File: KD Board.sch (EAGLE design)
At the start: 10 parts, among them IC1 LM555D

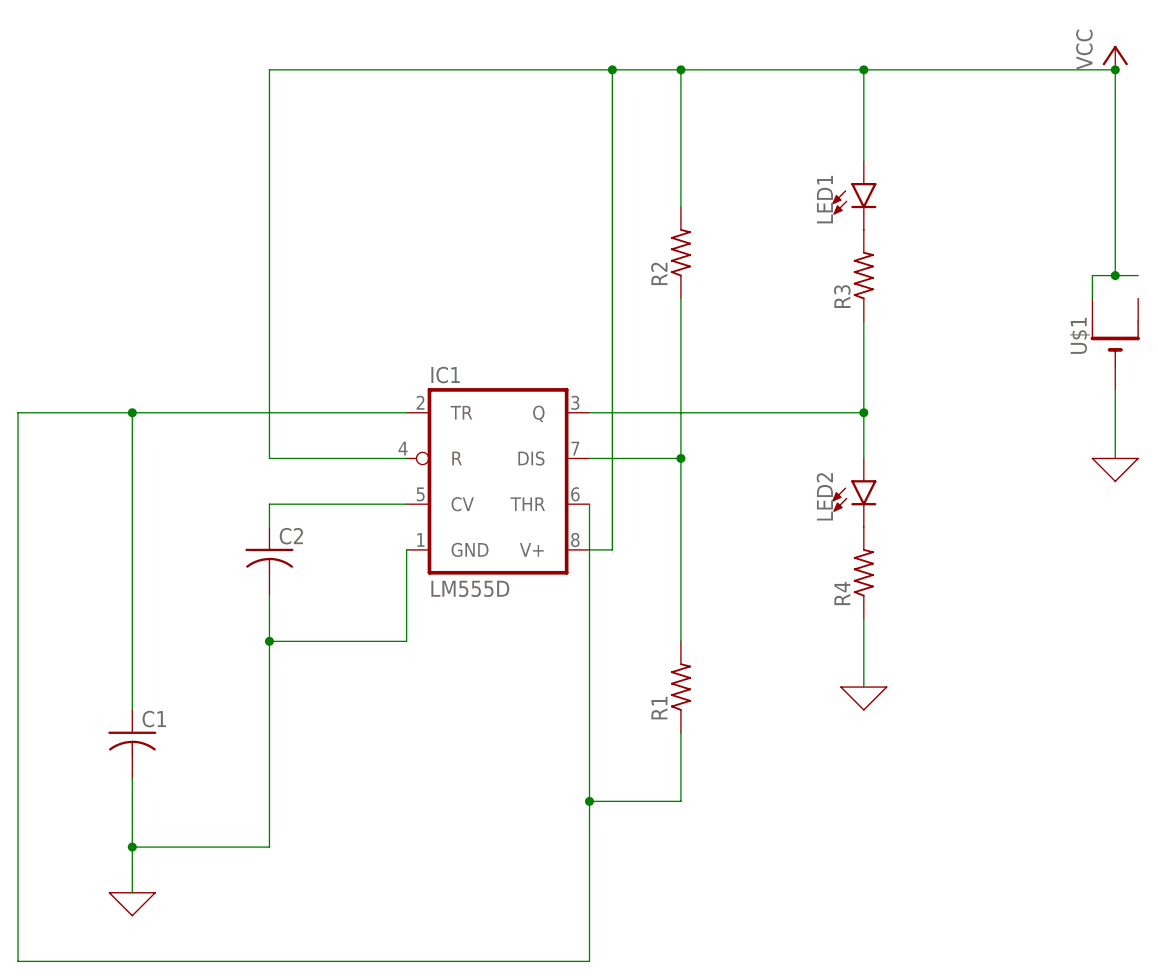
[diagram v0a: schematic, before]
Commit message: Moved name to silk layer. Board not square. Minor fixes.
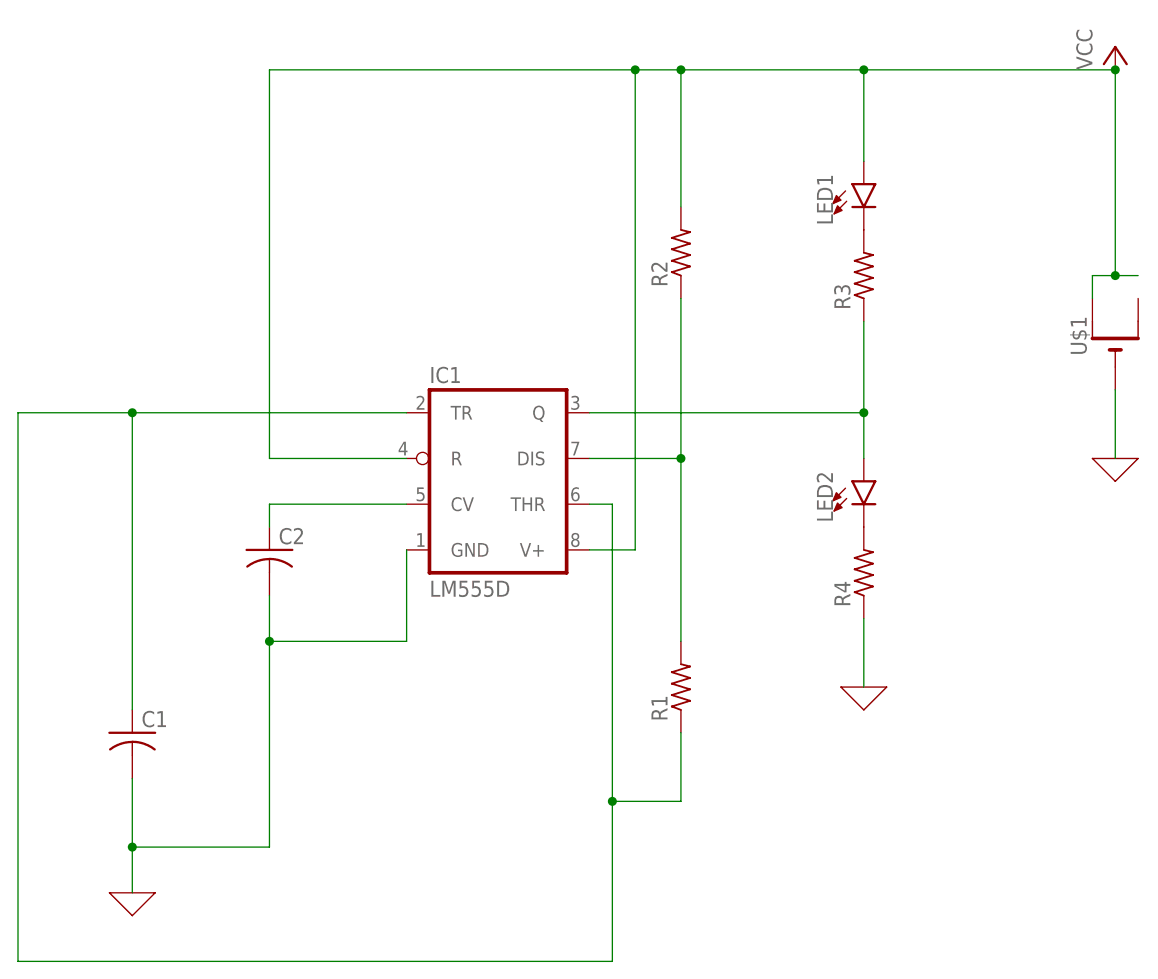
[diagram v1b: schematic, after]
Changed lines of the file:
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@@
 <wire x1="-10.16" y1="58.42" x2="-22.86" y2="58.42" width="0.1524" layer="91"/>
 <wire x1="-22.86" y1="58.42" x2="-22.86" y2="-2.54" width="0.1524" layer="91"/>
-<wire x1="-22.86" y1="-2.54" x2="40.64" y2="-2.54" width="0.1524" layer="91"/>
+<wire x1="-22.86" y1="-2.54" x2="43.18" y2="-2.54" width="0.1524" layer="91"/>
 <pinref part="IC1" gate="A" pin="THR"/>
-<wire x1="40.64" y1="48.26" x2="40.64" y2="15.24" width="0.1524" layer="91"/>
+<wire x1="40.64" y1="48.26" x2="43.18" y2="48.26" width="0.1524" layer="91"/>
+<wire x1="43.18" y1="48.26" x2="43.18" y2="15.24" width="0.1524" layer="91"/>
 <pinref part="R1" gate="G$1" pin="1"/>
-<wire x1="40.64" y1="15.24" x2="50.8" y2="15.24" width="0.1524" layer="91"/>
+<wire x1="43.18" y1="15.24" x2="50.8" y2="15.24" width="0.1524" layer="91"/>
 <wire x1="50.8" y1="15.24" x2="50.8" y2="22.86" width="0.1524" layer="91"/>
-<junction x="40.64" y="15.24"/>
-<wire x1="40.64" y1="-2.54" x2="40.64" y2="15.24" width="0.1524" layer="91"/>
+<junction x="43.18" y="15.24"/>
+<wire x1="43.18" y1="-2.54" x2="43.18" y2="15.24" width="0.1524" layer="91"/>
 </segment>
 </net>
@@
 <wire x1="20.32" y1="53.34" x2="5.08" y2="53.34" width="0.1524" layer="91"/>
 <wire x1="5.08" y1="53.34" x2="5.08" y2="96.52" width="0.1524" layer="91"/>
-<wire x1="5.08" y1="96.52" x2="43.18" y2="96.52" width="0.1524" layer="91"/>
+<wire x1="5.08" y1="96.52" x2="45.72" y2="96.52" width="0.1524" layer="91"/>
 <pinref part="IC1" gate="A" pin="V+"/>
-<wire x1="43.18" y1="96.52" x2="43.18" y2="43.18" width="0.1524" layer="91"/>
-<wire x1="43.18" y1="43.18" x2="40.64" y2="43.18" width="0.1524" layer="91"/>
-<wire x1="43.18" y1="96.52" x2="50.8" y2="96.52" width="0.1524" layer="91"/>
-<junction x="43.18" y="96.52"/>
+<wire x1="45.72" y1="96.52" x2="45.72" y2="43.18" width="0.1524" layer="91"/>
+<wire x1="45.72" y1="43.18" x2="40.64" y2="43.18" width="0.1524" layer="91"/>
+<wire x1="45.72" y1="96.52" x2="50.8" y2="96.52" width="0.1524" layer="91"/>
+<junction x="45.72" y="96.52"/>
 <pinref part="R2" gate="G$1" pin="2"/>
 <wire x1="50.8" y1="96.52" x2="50.8" y2="81.28" width="0.1524" layer="91"/>
@@
 </sheet>
 </sheets>
+<errors>
+</errors>
 </schematic>
 </drawing>
